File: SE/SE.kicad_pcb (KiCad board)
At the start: 2 copper layers, 42.9 x 35.1 mm, 16 parts, among them J1 RJ45, J2 Conn_01x04_Female, J3 Conn_01x03_Female, Q4 BC548

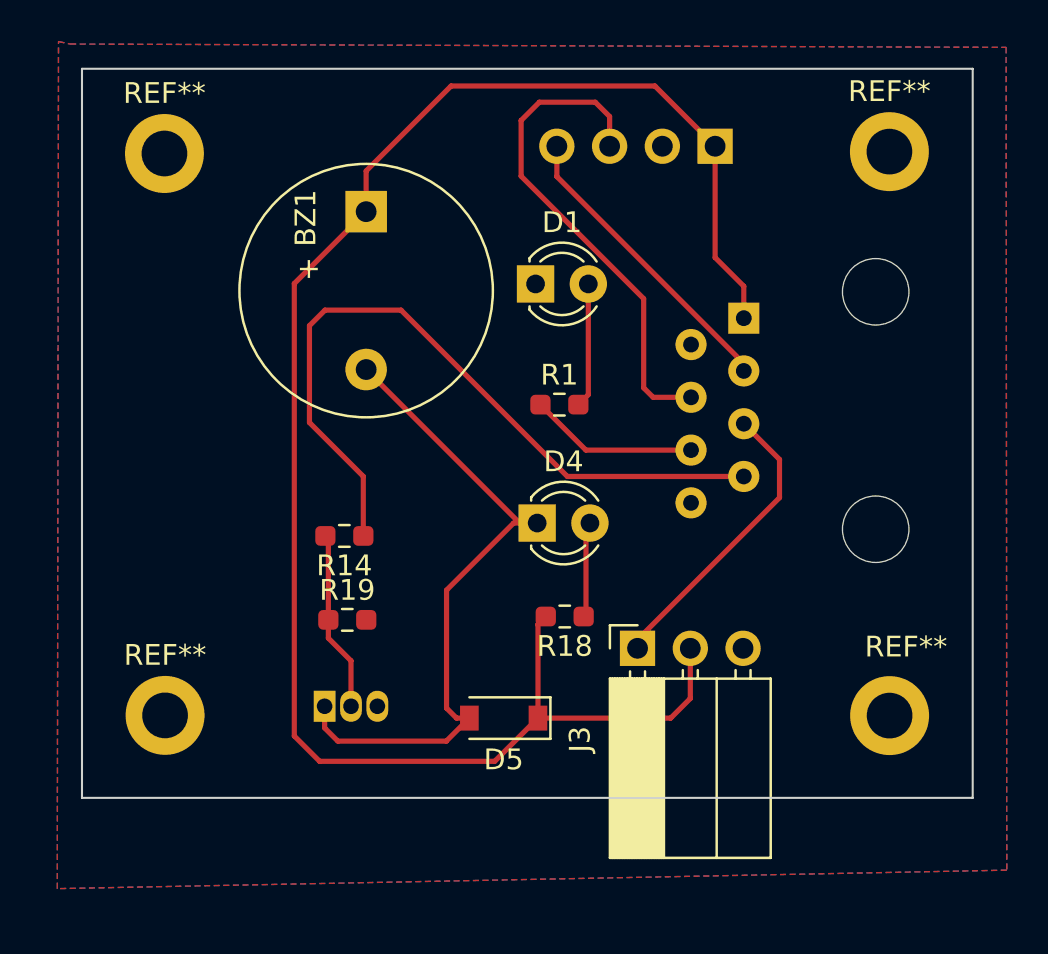
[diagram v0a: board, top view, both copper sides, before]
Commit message: Caja dinal sin tornillos
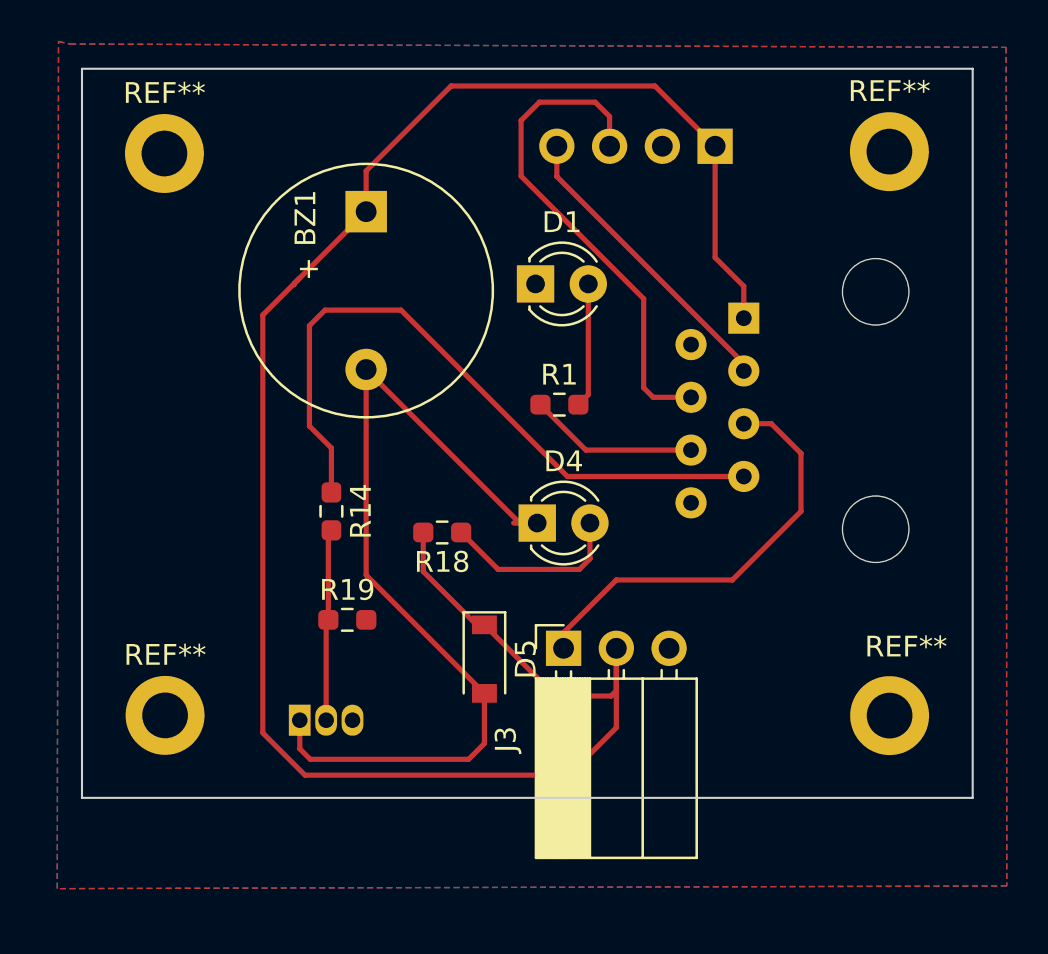
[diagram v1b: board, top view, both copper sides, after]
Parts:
- moved R18 7.15 mm to (54.1, 57.4)
- moved J3 3.56 mm to (59.9, 63.0)
- moved D5 2.99 mm to (56.1, 63.5), turned to -90 degrees
- moved Q4 1.37 mm to (47.2, 66.4)
- moved R14 1.34 mm to (48.8, 56.4), turned to -90 degrees
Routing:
- net +3.3V: track 85.5 -> 96.5 mm
- net Net-(BZ1-Pad2): track 32.3 -> 43.2 mm
- net Botones: track 14.4 -> 20.7 mm
- net Net-(D4-Pad2): track 4.55 -> 8.87 mm
- net Buzzer: track 35.7 -> 33.0 mm
- net Net-(Q4-Pad2): track 8.71 -> 9.45 mm

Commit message: PCB
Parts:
- removed the REF** at (40.7, 39.2)
- J2: moved to F.Cu
- moved J2 28.6 mm to (38.6, 37.8)
- moved BZ1 12.5 mm to (39.1, 47.2), turned to 0 degrees
- moved D5 9.74 mm to (54.9, 53.8), turned to 180 degrees
- moved Q4 9.39 mm to (48.6, 57.1), turned to -90 degrees
- moved R14 4.77 mm to (53.1, 58.4), turned to 180 degrees
- moved R18 3.88 mm to (57.4, 59.4), turned to -90 degrees
- moved R19 3.30 mm to (52.8, 61.7), turned to -90 degrees
- moved D1 3.13 mm to (61.5, 44.2), turned to -90 degrees
- moved D4 3.09 mm to (61.5, 55.6), turned to -90 degrees
- moved R1 1.78 mm to (61.5, 50.8)
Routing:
- net SDA: track 14.5 -> 38.5 mm
- net SCL: track 24.1 -> 47.0 mm
- net Net-(BZ1-Pad2): track 43.2 -> 28.1 mm
- net Buzzer: track 33.0 -> 26.9 mm
- net +3.3V: track 96.5 -> 101.3 mm
- net Net-(D4-Pad2): track 8.87 -> 4.21 mm
- net Botones: track 20.7 -> 16.8 mm
- net Net-(Q4-Pad2): track 9.45 -> 6.22 mm
- net (no net): track 0.00 -> 1.27 mm
- net Net-(D1-Pad2): track 6.01 -> 4.95 mm

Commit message: PCB
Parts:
- moved Q4 1.78 mm to (46.8, 57.1)
- moved R19 1.05 mm to (53.1, 62.7), turned to 180 degrees
- moved R1 0.36 mm to (61.5, 50.4), turned to 90 degrees
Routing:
- net Net-(Q4-Pad2): track 6.22 -> 10.4 mm
- net Led_Verde: track 7.71 -> 5.60 mm
- net (no net): track 1.27 -> 0.00 mm
- net Net-(BZ1-Pad2): track 28.1 -> 27.0 mm
- net Net-(D1-Pad2): track 4.95 -> 4.07 mm
- net Buzzer: track 26.9 -> 27.5 mm
